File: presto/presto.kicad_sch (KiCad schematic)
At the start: 6 parts, among them J101 12V IN

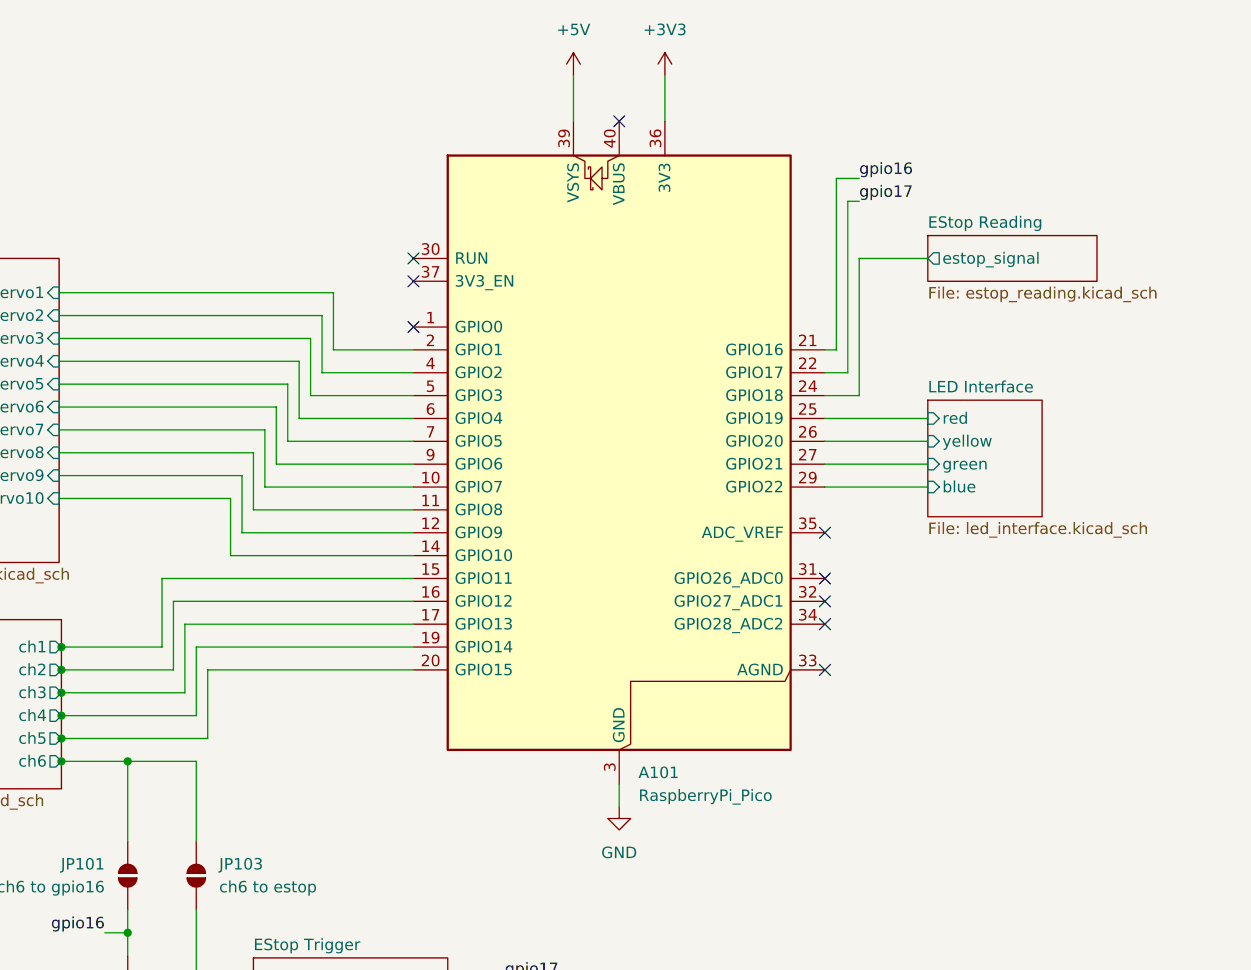
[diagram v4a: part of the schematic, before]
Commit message: 2-pin JST added for autonomous, 6 routes not connected for some reason though
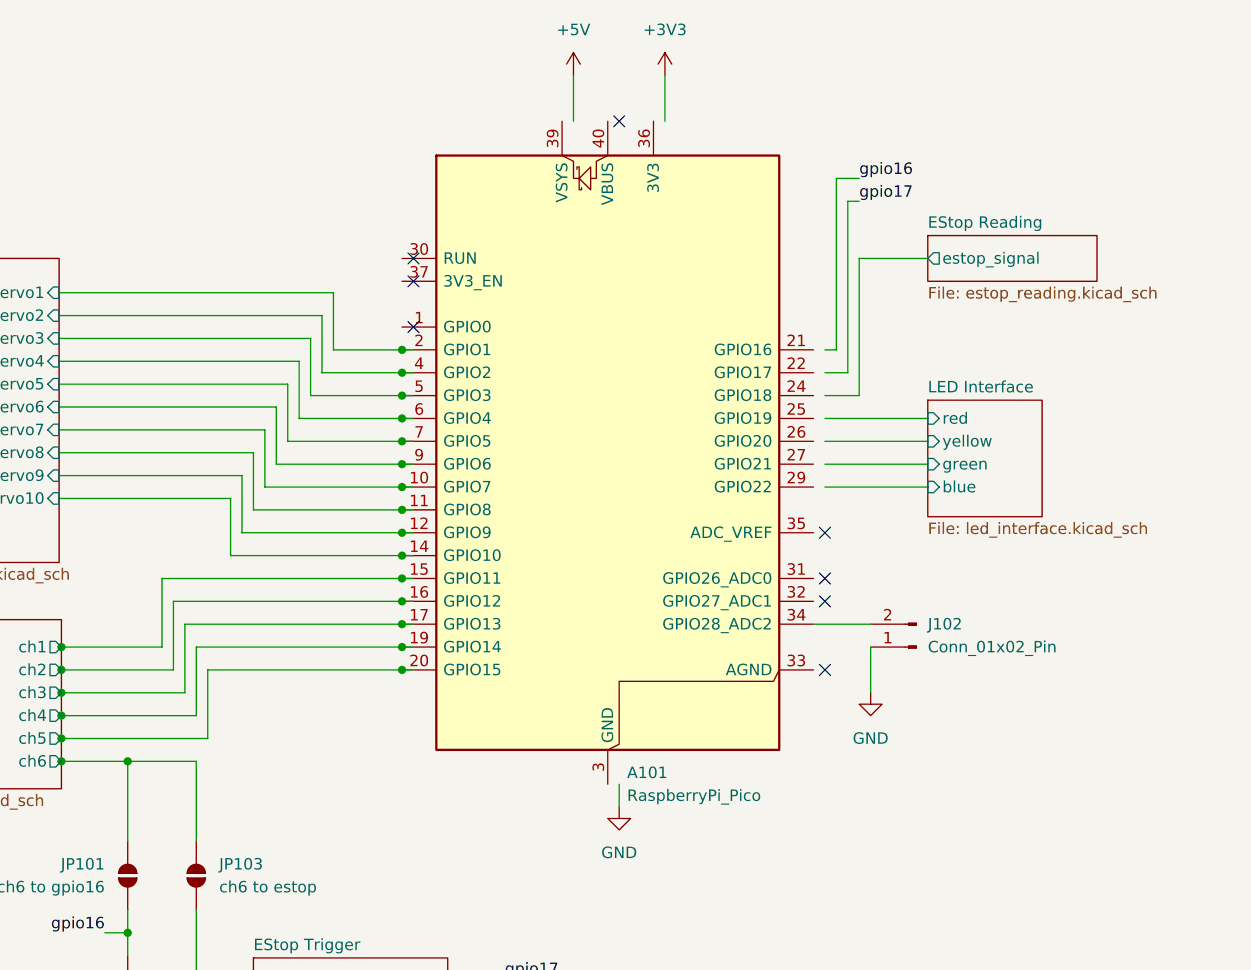
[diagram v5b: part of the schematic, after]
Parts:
- added J102: Conn_01x02_Pin, Connector_JST:JST_XH_B2B-XH-A_1x02_P2.50mm_Vertical, symbol Connector:Conn_01x02_Pin
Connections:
- net +3V3: no longer A101.36 (3V3)
- net +5V: no longer A101.39 (VSYS)
- net EStop Reading/estop_signal: no longer A101.24 (GPIO18)
- net GND: now also J102.1 (Pin_1); no longer A101.13 (GND), A101.18 (GND), A101.23 (GND), A101.28 (GND), A101.3 (GND), A101.38 (GND), A101.8 (GND)
- net LED Interface/blue: no longer A101.29 (GPIO22)
- net LED Interface/green: no longer A101.27 (GPIO21)
- net LED Interface/red: no longer A101.25 (GPIO19)
- net LED Interface/yellow: no longer A101.26 (GPIO20)
- net gpio16: no longer A101.21 (GPIO16)
- net gpio17: no longer A101.22 (GPIO17)
- net at A101.34 (GPIO28_ADC2): now also J102.2 (Pin_2)
- new net: A101.13 (GND), A101.18 (GND), A101.23 (GND), A101.28 (GND), A101.3 (GND), A101.38 (GND), A101.8 (GND)
- no-connect marks 9 -> 8
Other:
- moved on the sheet: A101

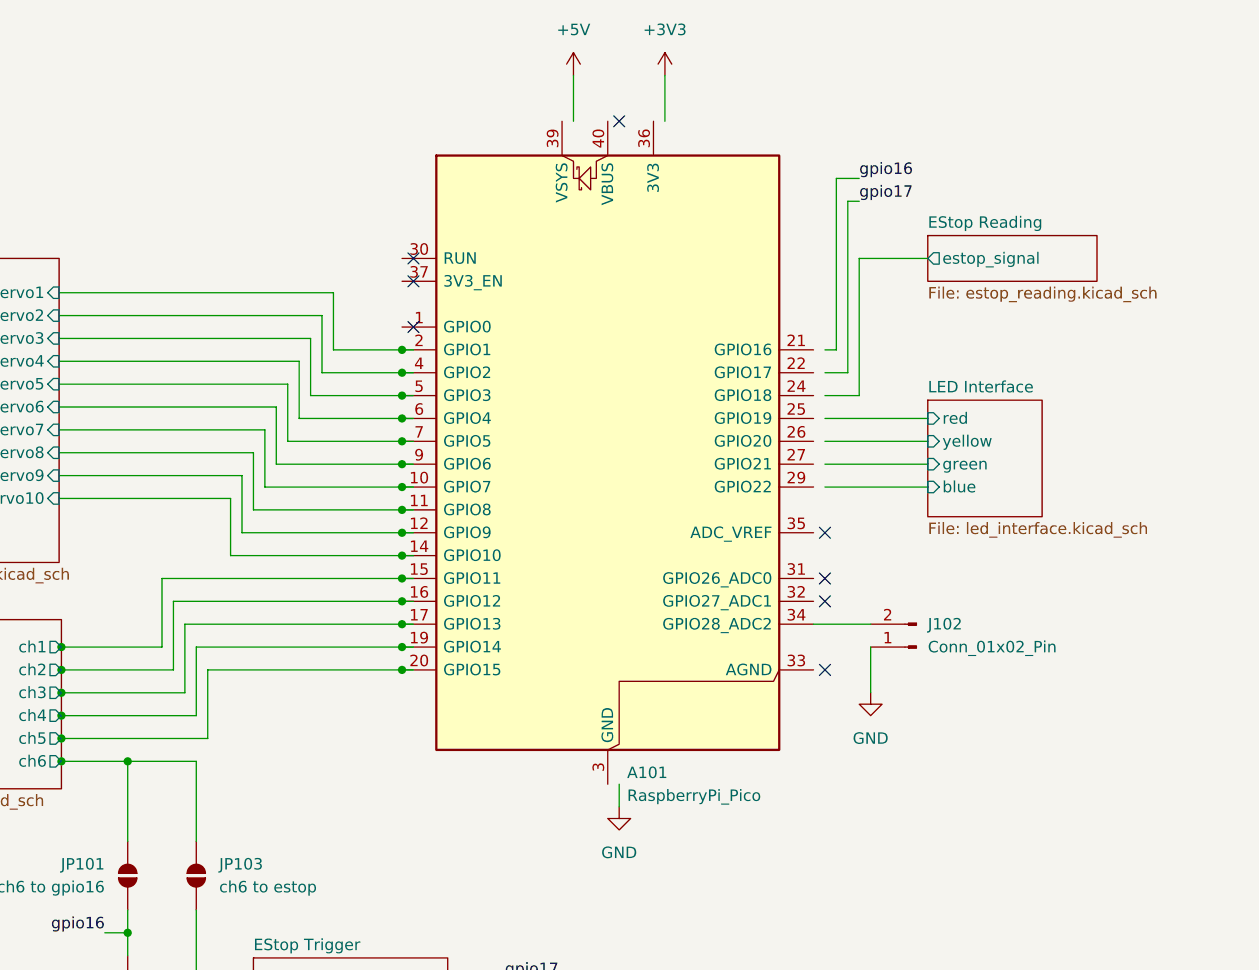
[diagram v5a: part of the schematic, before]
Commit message: added connector for neopixel and fixed autonomy switch layout
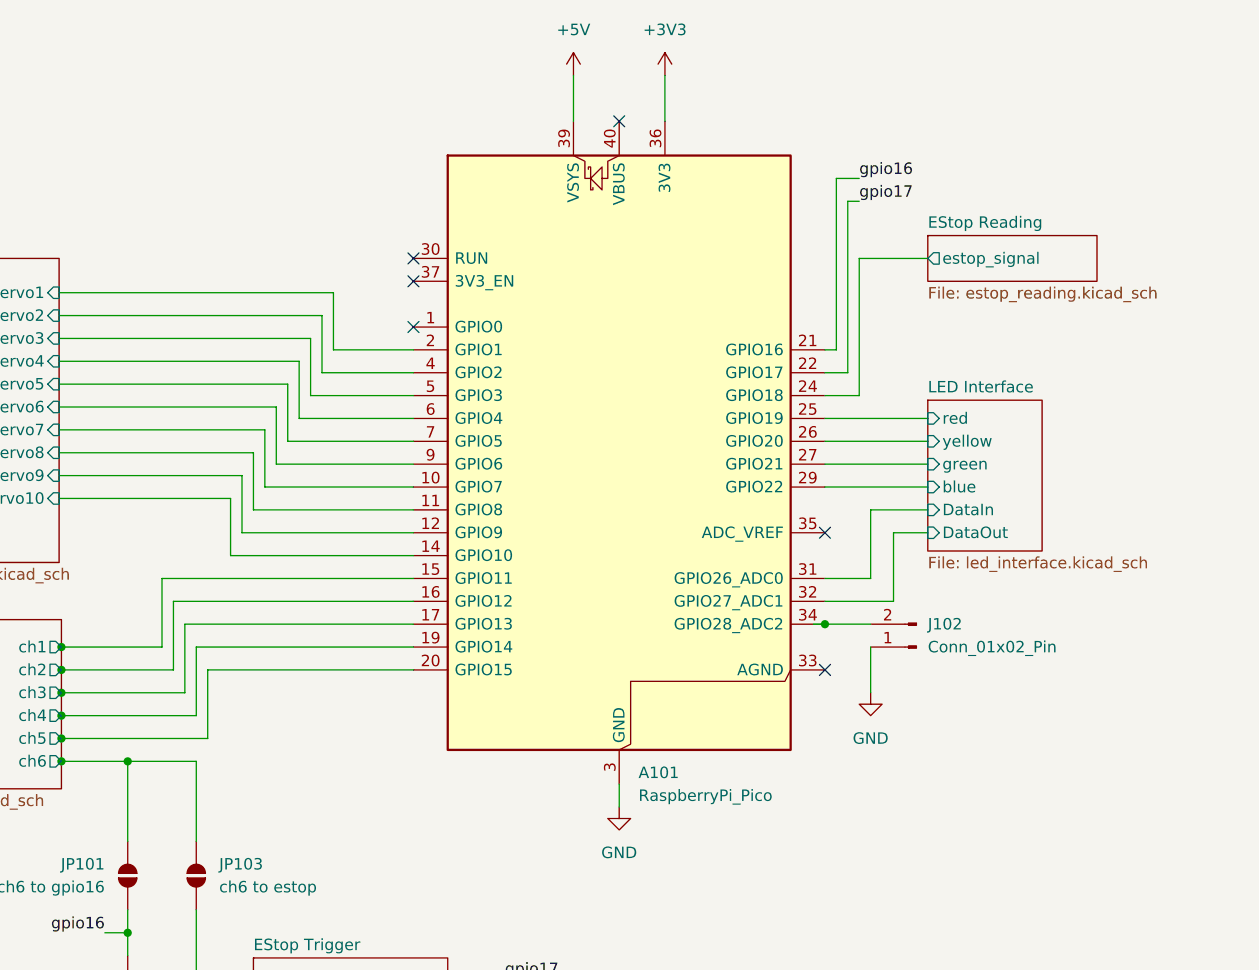
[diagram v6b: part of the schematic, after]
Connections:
- net +3V3: now also A101.36 (3V3)
- net +5V: now also A101.39 (VSYS)
- net EStop Reading/estop_signal: now also A101.24 (GPIO18)
- net GND: now also A101.13 (GND), A101.18 (GND), A101.23 (GND), A101.28 (GND), A101.3 (GND), A101.38 (GND), A101.8 (GND)
- net LED Interface/blue: now also A101.29 (GPIO22)
- net LED Interface/green: now also A101.27 (GPIO21)
- net LED Interface/red: now also A101.25 (GPIO19)
- net LED Interface/yellow: now also A101.26 (GPIO20)
- net gpio16: now also A101.21 (GPIO16)
- net gpio17: now also A101.22 (GPIO17)
- net LED Interface/DataIn: now reaches A101.31 (GPIO26_ADC0)
- net LED Interface/DataOut: now reaches A101.32 (GPIO27_ADC1)
- no-connect marks 8 -> 6
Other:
- sheet LED Interface ports: added DataIn, DataOut; removed none
- moved on the sheet: A101
